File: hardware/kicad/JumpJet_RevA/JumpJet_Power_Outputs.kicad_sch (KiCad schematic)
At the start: 44 parts, among them J1 24V IN / 20A MIN, J2 PTC 24V / 200W, J3 4-WIRE FAN: 24V/GND/TACH/PWM, J4 AUX1 DNP, Q1 60V NFET TBD, Q2 2N7002-CLASS PWM OD PROVISION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, Q3 60V NFET DNP, Q4 Q_GATE_EN 2N7002-CLASS PROVIS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, U1 SN74LV4T125

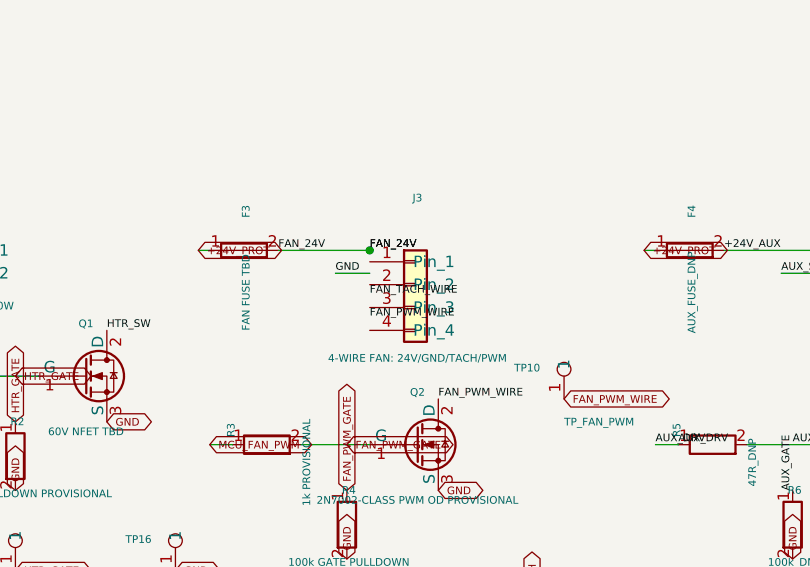
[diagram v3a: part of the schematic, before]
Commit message: hardware: connect Rev A fan header
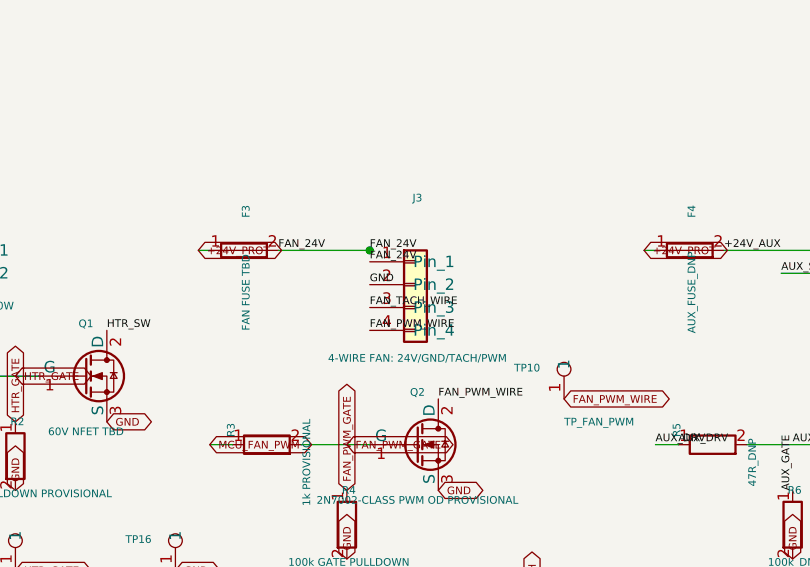
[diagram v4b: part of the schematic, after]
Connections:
- net FAN_24V: now also J3.1 (Pin_1)
- net FAN_PWM_WIRE: now also J3.4 (Pin_4)
- net FAN_TACH_WIRE: now also J3.3 (Pin_3)
- net GND: now also J3.2 (Pin_2)
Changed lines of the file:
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@@
-    (stroke (width 0) (type default))
-  )
-  (wire (pts (xy 264.16 55.88) (xy 267.97 55.88))
     (stroke (width 0) (type default))
   )
@@
     (effects (font (size 0.95 0.95) (thickness 0.120)) (justify left bottom))
   )
-  (label "GND" (at 264.16 55.88 0)
+  (label "GND" (at 267.97 57.15 0)
     (effects (font (size 0.85 0.85)) (justify left bottom))
   )
@@
     (effects (font (size 0.85 0.85)) (justify left bottom))
   )
-  (label "FAN_24V" (at 267.97 53.34 0)
+  (label "FAN_24V" (at 267.97 54.61 0)
     (effects (font (size 0.85 0.85)) (justify left bottom))
   )
-  (label "FAN_TACH_WIRE" (at 267.97 58.42 0)
+  (label "FAN_TACH_WIRE" (at 267.97 59.69 0)
     (effects (font (size 0.85 0.85)) (justify left bottom))
   )
-  (label "FAN_PWM_WIRE" (at 267.97 60.96 0)
+  (label "FAN_PWM_WIRE" (at 267.97 62.23 0)
     (effects (font (size 0.85 0.85)) (justify left bottom))
   )
